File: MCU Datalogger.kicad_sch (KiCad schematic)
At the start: 25 parts, among them U1 24LC1025, U2 24LC1025, U3 DS1337S_, U4 ATMEGA328P-AU, Y1 16MHz, Y2 32.768 KHz

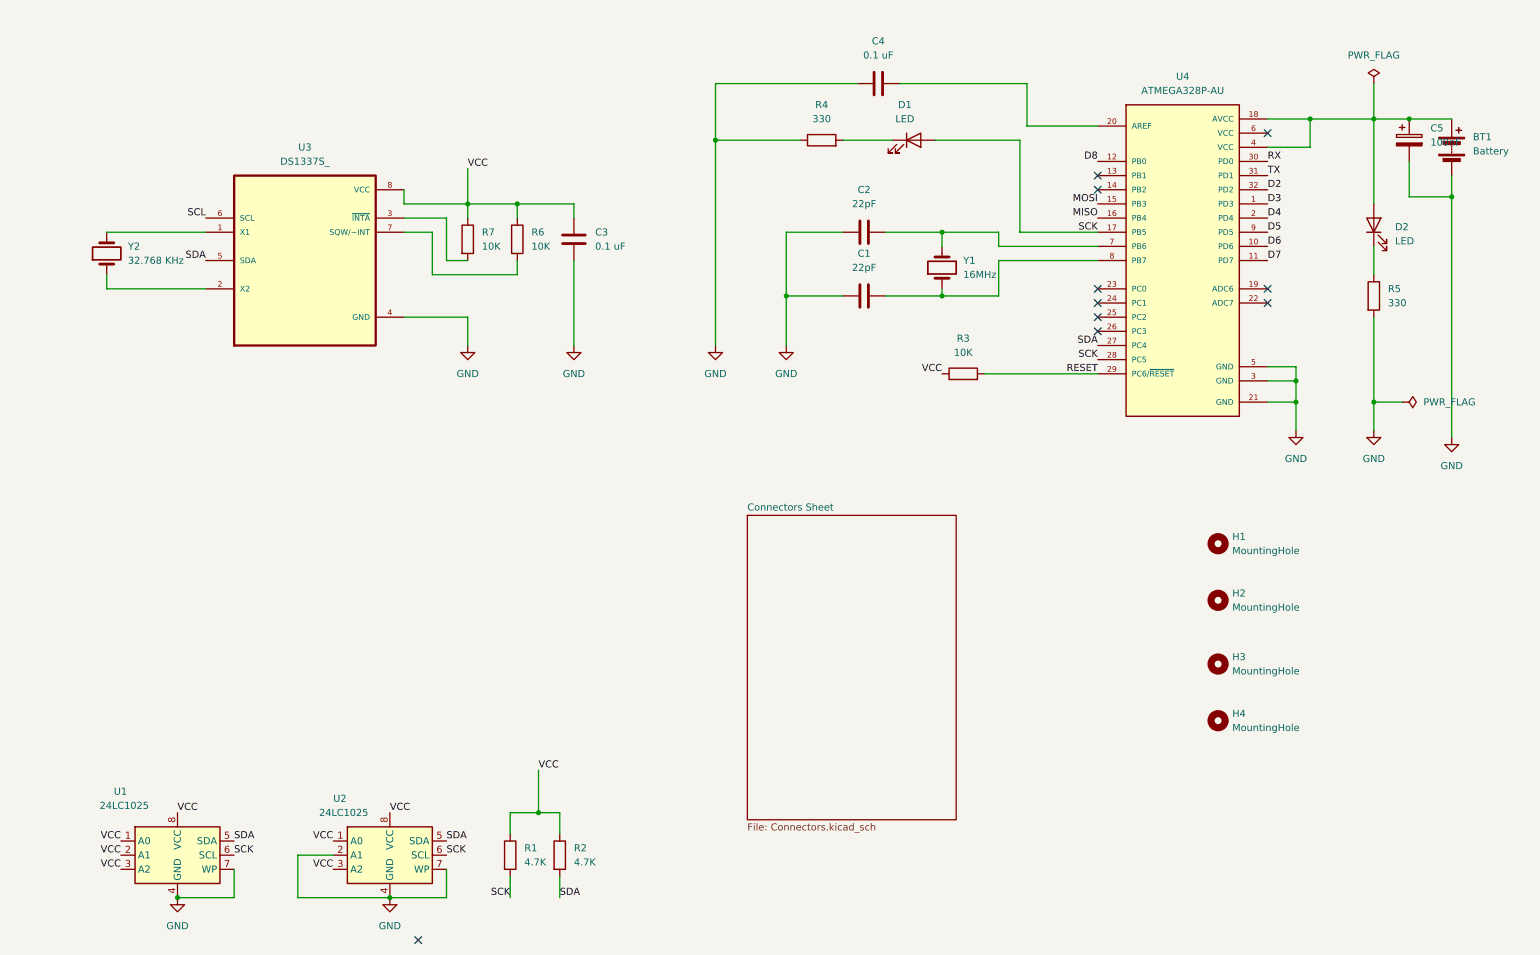
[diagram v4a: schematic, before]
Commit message: Updated wiring of both sheets
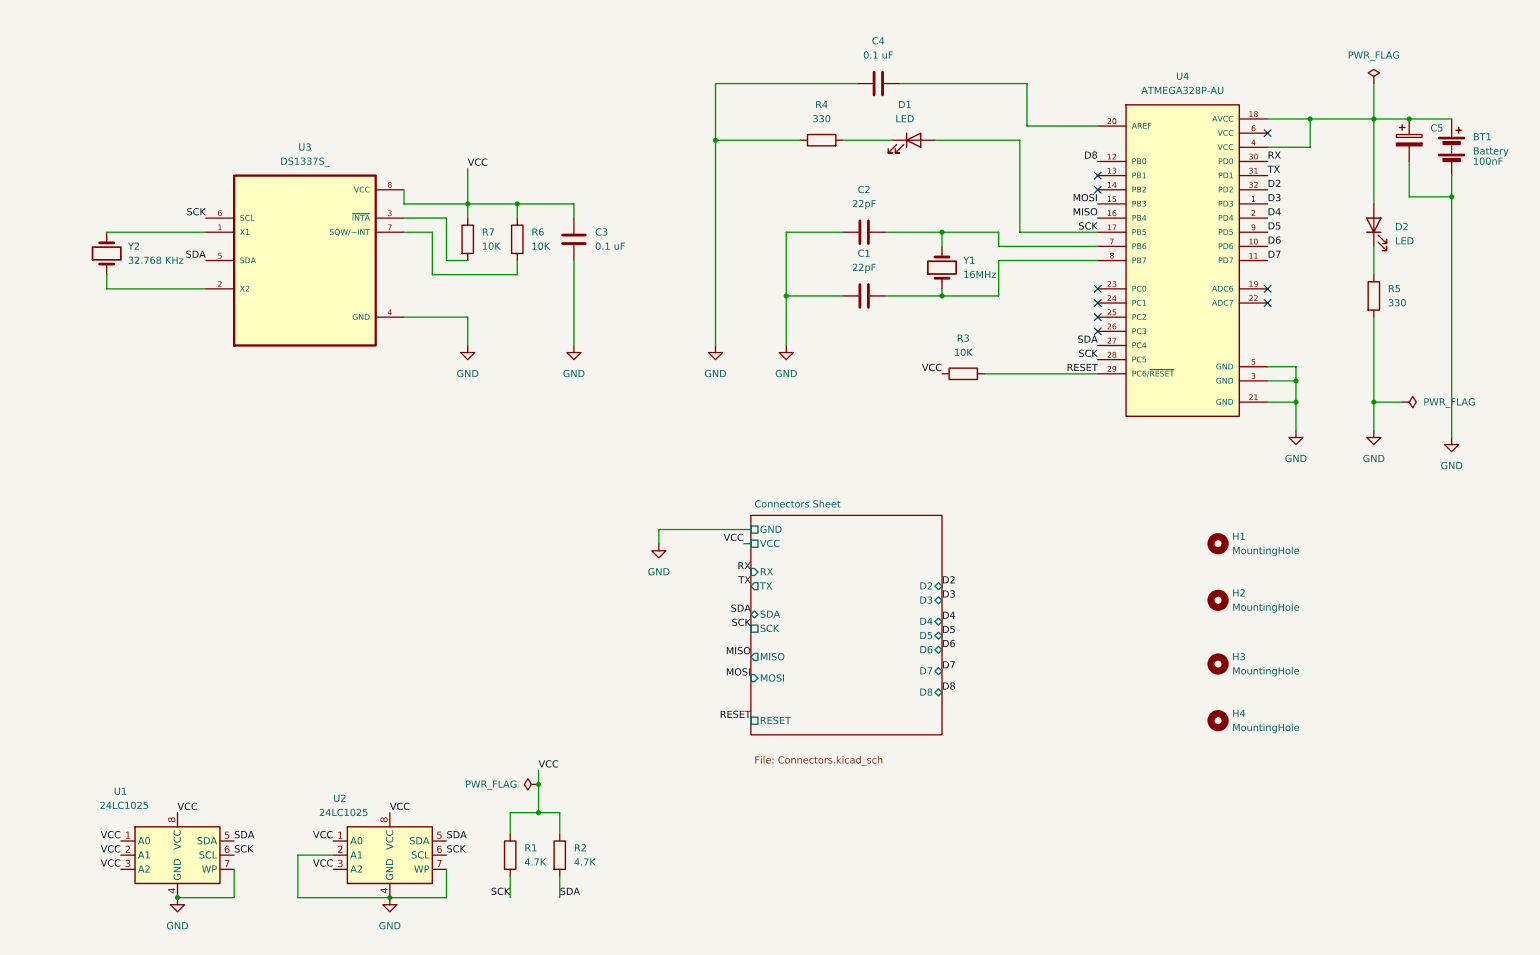
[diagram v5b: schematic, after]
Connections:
- net SCL is gone; now on net SCK: U3.6 (SCL)
- no-connect marks 10 -> 9
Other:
- sheet Connectors Sheet ports: added D2, D3, D4, D5, D6, D7, D8, GND, MISO, MOSI, RESET, RX, SCK, SDA, TX, VCC; removed none

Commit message: Completed comments
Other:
- note added: "EPROM"
- note added: "MCU"
- note added: "Mounting Holes"
- note added: "Real Time Clock"
- moved on the sheet: C3, H1, H2, H3, H4, R1, R2, R6, R7, U1, U2, U3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
